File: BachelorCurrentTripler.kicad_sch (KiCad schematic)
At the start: 5 parts, among them J1 Conn_01x07_Pin, J2 Conn_01x01_Pin, J3 Conn_01x01_Pin, J4 Conn_01x04_Socket, J5 Conn_01x01_Pin

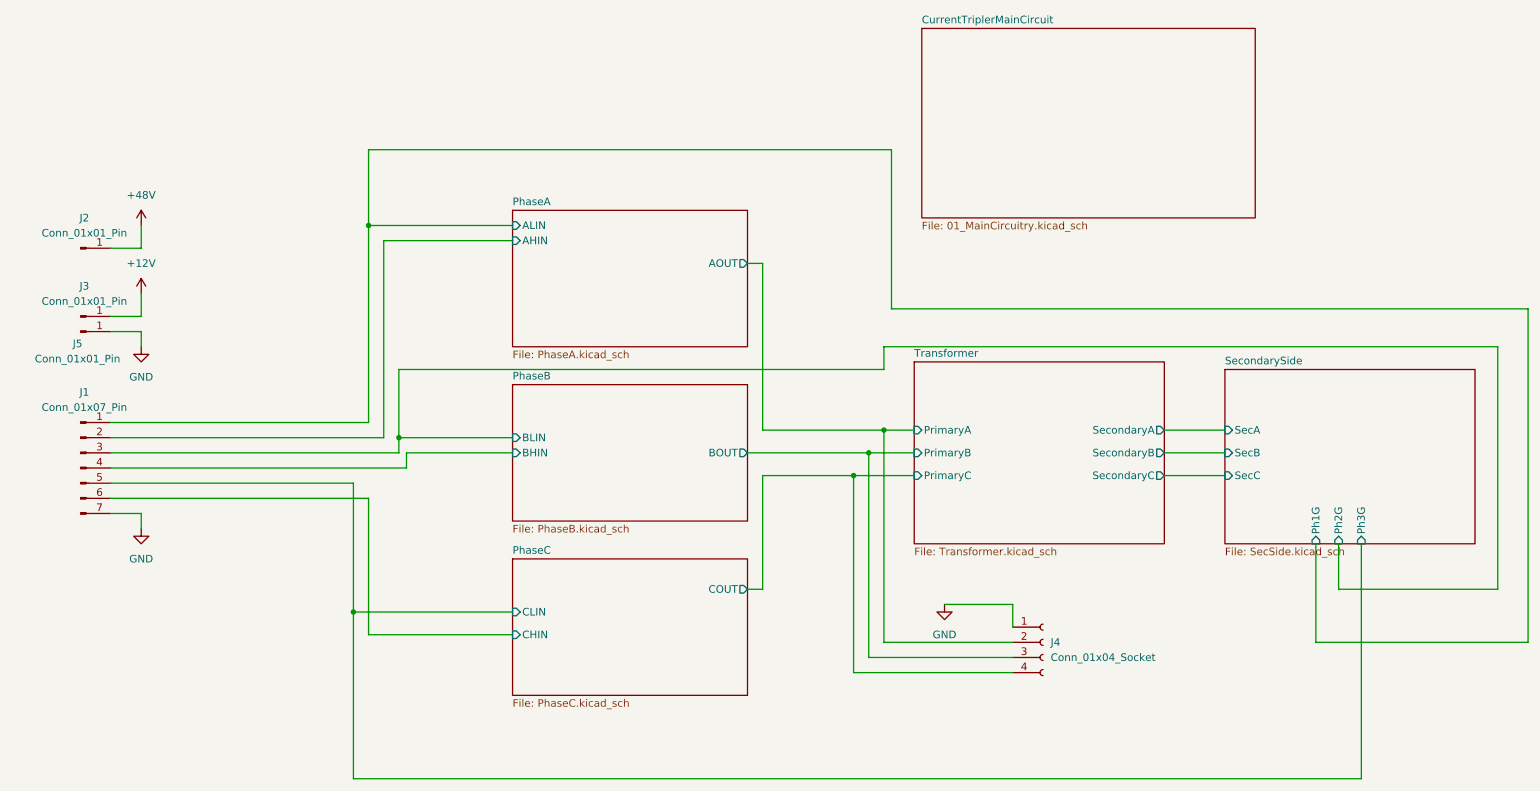
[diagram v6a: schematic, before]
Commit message: all små komponenter er nu 0805, og jeg har fixet strømmen under kondensatorerene, mangler kun at bytte rundt på 12Vin og GND
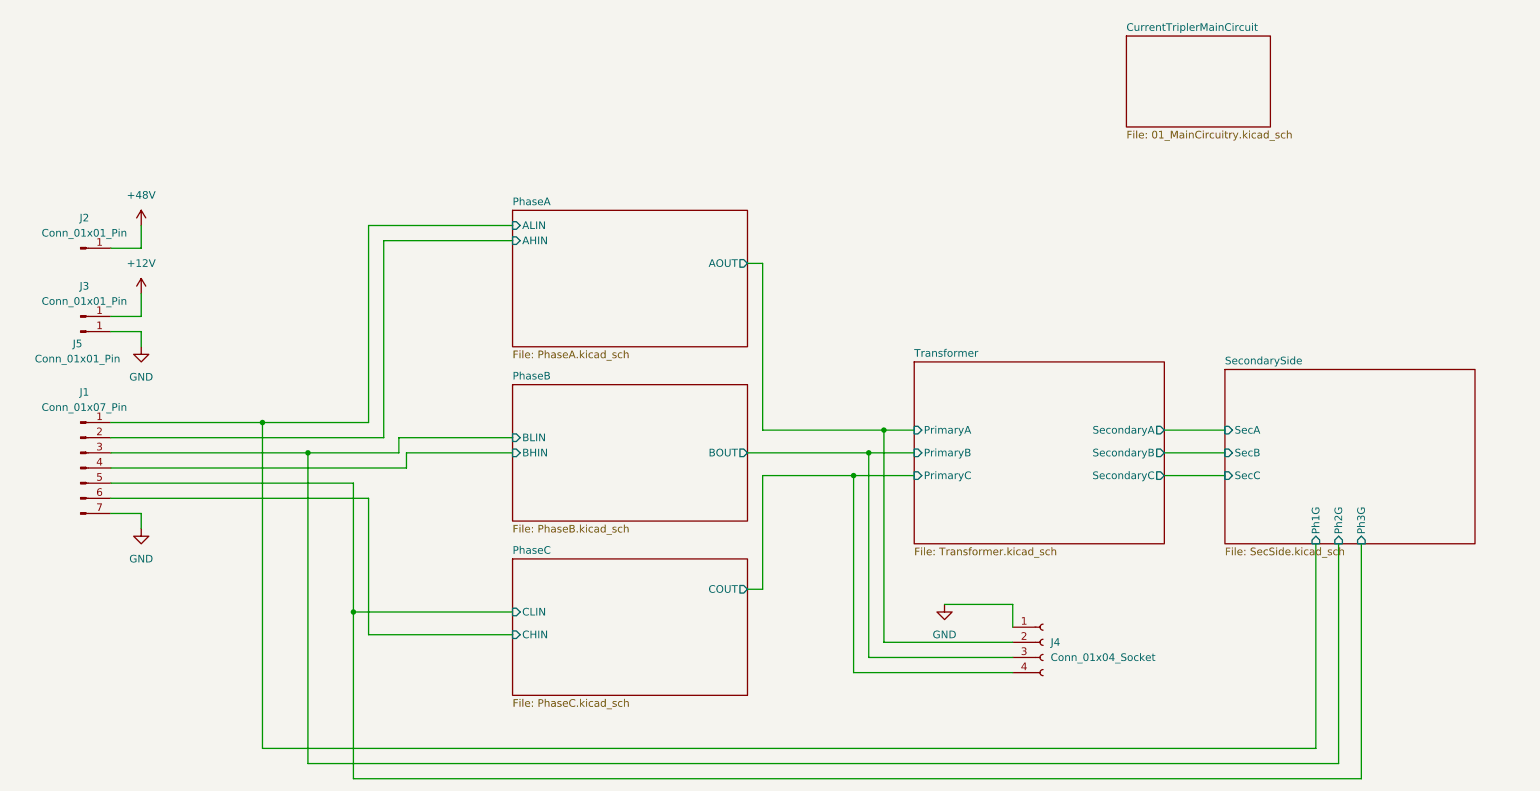
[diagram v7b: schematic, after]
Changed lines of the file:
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@@
 	(paper "A4")
 	(junction
-		(at 86.36 52.07)
+		(at 68.58 85.09)
 		(diameter 0)
 		(color 0 0 0 0)
@@
 	)
 	(junction
-		(at 91.44 87.63)
+		(at 76.2 90.17)
 		(diameter 0)
 		(color 0 0 0 0)
@@
 	(wire
 		(pts
+			(xy 68.58 139.7) (xy 245.11 139.7)
+		)
+		(stroke
+			(width 0)
+			(type default)
+		)
+	)
+	(wire
+		(pts
+			(xy 76.2 90.17) (xy 91.44 90.17)
+		)
+		(stroke
+			(width 0)
+			(type default)
+		)
+	)
+	(wire
+		(pts
 			(xy 194.31 115.57) (xy 194.31 119.38)
 		)
@@
 	(wire
 		(pts
-			(xy 275.59 72.39) (xy 275.59 113.03)
-		)
-		(stroke
-			(width 0)
-			(type default)
-		)
-	)
-	(wire
-		(pts
-			(xy 172.72 72.39) (xy 275.59 72.39)
-		)
-		(stroke
-			(width 0)
-			(type default)
-		)
-	)
-	(wire
-		(pts
 			(xy 149.86 90.17) (xy 170.18 90.17)
 		)
@@
 	(wire
 		(pts
-			(xy 91.44 76.2) (xy 172.72 76.2)
-		)
-		(stroke
-			(width 0)
-			(type default)
-		)
-	)
-	(wire
-		(pts
 			(xy 152.4 93.98) (xy 167.64 93.98)
 		)
@@
 	(wire
 		(pts
-			(xy 172.72 76.2) (xy 172.72 72.39)
-		)
-		(stroke
-			(width 0)
-			(type default)
-		)
-	)
-	(wire
-		(pts
 			(xy 86.36 85.09) (xy 86.36 52.07)
 		)
@@
 	(wire
 		(pts
-			(xy 280.67 66.04) (xy 280.67 121.92)
-		)
-		(stroke
-			(width 0)
-			(type default)
-		)
-	)
-	(wire
-		(pts
 			(xy 152.4 58.42) (xy 152.4 86.36)
 		)
@@
 	(wire
 		(pts
-			(xy 280.67 121.92) (xy 245.11 121.92)
-		)
-		(stroke
-			(width 0)
-			(type default)
-		)
-	)
-	(wire
-		(pts
-			(xy 275.59 113.03) (xy 248.92 113.03)
+			(xy 68.58 85.09) (xy 86.36 85.09)
 		)
 		(stroke
@@
 	(wire
 		(pts
+			(xy 68.58 85.09) (xy 68.58 139.7)
+		)
+		(stroke
+			(width 0)
+			(type default)
+		)
+	)
+	(wire
+		(pts
 			(xy 152.4 86.36) (xy 172.72 86.36)
 		)
@@
 	(wire
 		(pts
-			(xy 86.36 39.37) (xy 173.99 39.37)
-		)
-		(stroke
-			(width 0)
-			(type default)
-		)
-	)
-	(wire
-		(pts
 			(xy 167.64 93.98) (xy 177.8 93.98)
 		)
@@
 	(wire
 		(pts
-			(xy 86.36 52.07) (xy 86.36 39.37)
-		)
-		(stroke
-			(width 0)
-			(type default)
-		)
-	)
-	(wire
-		(pts
-			(xy 173.99 66.04) (xy 280.67 66.04)
+			(xy 76.2 90.17) (xy 76.2 142.24)
 		)
 		(stroke
@@
 	(wire
 		(pts
+			(xy 76.2 142.24) (xy 248.92 142.24)
+		)
+		(stroke
+			(width 0)
+			(type default)
+		)
+	)
+	(wire
+		(pts
 			(xy 92.71 92.71) (xy 92.71 90.17)
 		)
@@
 	(wire
 		(pts
-			(xy 245.11 121.92) (xy 245.11 105.41)
+			(xy 245.11 105.41) (xy 245.11 139.7)
 		)
 		(stroke
@@
 	(wire
 		(pts
-			(xy 91.44 87.63) (xy 91.44 76.2)
-		)
-		(stroke
-			(width 0)
-			(type default)
-		)
-	)
-	(wire
-		(pts
-			(xy 43.18 90.17) (xy 91.44 90.17)
+			(xy 43.18 90.17) (xy 76.2 90.17)
 		)
 		(stroke
@@
 	(wire
 		(pts
-			(xy 43.18 85.09) (xy 86.36 85.09)
+			(xy 43.18 85.09) (xy 68.58 85.09)
 		)
 		(stroke
@@
 	(wire
 		(pts
-			(xy 173.99 39.37) (xy 173.99 66.04)
-		)
-		(stroke
-			(width 0)
-			(type default)
-		)
-	)
-	(wire
-		(pts
-			(xy 248.92 113.03) (xy 248.92 105.41)
+			(xy 248.92 105.41) (xy 248.92 142.24)
 		)
 		(stroke
@@
 	)
 	(sheet
-		(at 179.07 19.05)
-		(size 55.88 31.75)
+		(at 213.36 20.32)
+		(size 24.13 15.24)
 		(exclude_from_sim no)
 		(in_bom yes)
@@
 		)
 		(property "Sheetname" "CurrentTriplerMainCircuit"
-			(at 179.07 18.3384 0)
+			(at 213.36 19.6084 0)
 			(effects
 				(font
@@
 		)
 		(property "Sheetfile" "01_MainCircuitry.kicad_sch"
-			(at 179.07 51.3846 0)
-			(effects
-				(font
+			(at 213.36 36.1446 0)
+			(effects
+				(font
